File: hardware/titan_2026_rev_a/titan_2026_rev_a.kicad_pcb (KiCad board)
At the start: 2 copper layers, 82 x 56 mm, 86 parts, among them J1 DS1023-2*20SF11, J10 XT30PW-F30.G.Y, J11 XT30PW-M30.G.Y, J12 BWSMA-KWE-Z001, J2 B5B-XH, J3 B5B-XH, J4 B3B-XH, J5 B3B-XH, J6 HB-PH9-12727PB2GOB, J7 B7B-XH, J8 B7B-XH, J9 USB4105-GF-A-120, SW1 SW_SPST, U1 BME280, U10 TPS2116DRL, U11 ATGM336H-5N31, U12 NRF24L01_Breakout, U13 AT2659S, U2 SCD41-D-R2, U3 STM32F105RCT6, U4 ISO1642DWR, U5 USBLC6-2SC6, U6 INA219AIDCN, U7 TLV73333PDBV, U8 TPS563201, U9 TPS2116DRL, Y1 8M

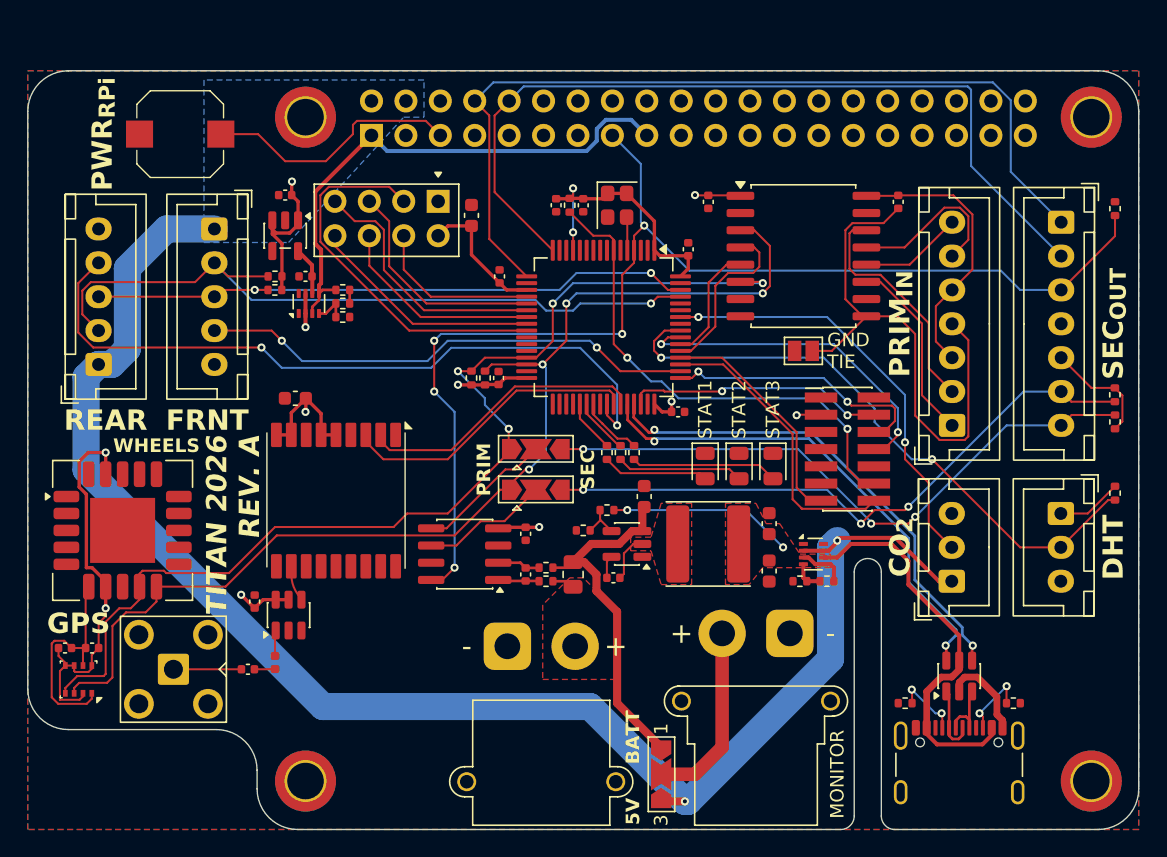
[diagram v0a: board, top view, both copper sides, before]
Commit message: Added more silkscreen annotations
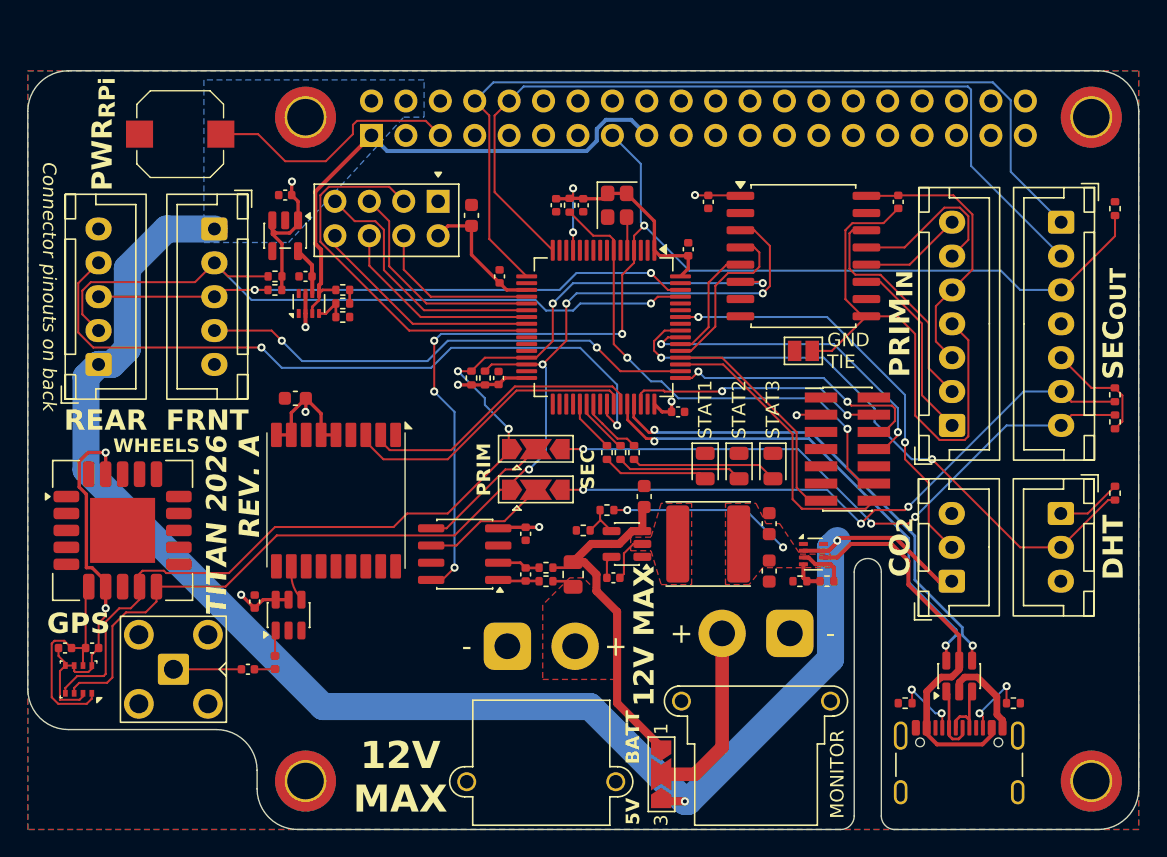
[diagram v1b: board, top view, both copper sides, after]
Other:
- board text added: "12V MAX"
- board text added: "3V3"
- board text added: "5-12V"
- board text added: "Can tolerate up to 17V but might damage displays"
- board text added: "Connector pinouts on back"
- board text added: "LET'S GO!"
- board text added: "REV. ${REVISION}"
- board text added: "SAVO WUZ HERE :)"
- board text added: "TITAN 2026 HAT"

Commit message: HAT Rev. A ready for ordering
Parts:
- added JP5: SolderJumper_3_Open, Jumper:SolderJumper-3_P2.0mm_Open_TrianglePad1.0x1.5mm, F.Cu at (76.2, 54.8)
- J10: value XT30PW-F30.G.Y -> XT30PW-F20.G.Y
- U6: footprint Package_SO:SOIC-8_3.9x4.9mm_P1.27mm -> Package_TO_SOT_SMD:SOT-23-8
- moved U6 1.50 mm to (106.5, 86.0)
- moved C22 1.00 mm to (109.5, 85.5)
- moved SW1 0.50 mm to (83.5, 55.0)
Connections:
- J2 pad 1: +5V -> /Sensors/PWR_{WHEEL}
- J3 pad 1: +5V -> /Sensors/PWR_{WHEEL}
- R6 pad 1: +5V -> /Sensors/PWR_{WHEEL}
- R7 pad 1: +5V -> /Sensors/PWR_{WHEEL}
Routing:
- net /Sensors/PWR_{WHEEL}: track 0.00 -> 37.6 mm
- net +5V: track 129.0 -> 138.3 mm, vias 3 -> 4
- net /Power/SDA: track 9.43 -> 7.09 mm
- net +3V3: track 106.4 -> 107.7 mm, vias 12 -> 13
- net /Power/SCL: track 10.1 -> 9.36 mm, vias 0 -> 2
- net /ROLE: track 89.7 -> 89.0 mm
- net /RPI_SW: track 19.1 -> 19.6 mm
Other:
- board text added: "3"
- board text added: "5"
- board text added: "PWR"
- board text added: "Set wheel power on top side! Start with 3(.3)V"
- board text added: "WHL PWR"
